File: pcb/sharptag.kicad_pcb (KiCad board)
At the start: 2 copper layers, 76.9 x 56.2 mm, 93 parts, among them J1 USB_C_Receptacle_USB2.0, J2 Conn_01x10, J3 Conn_01x02, J4 Conn_01x04, J5 Conn_01x03, J6 Conn_01x03, Q1 DMG3415U-7, Q2 DMG3415U-7, Q3 DMG3415U-7, Q4 Q_Photo_NPN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

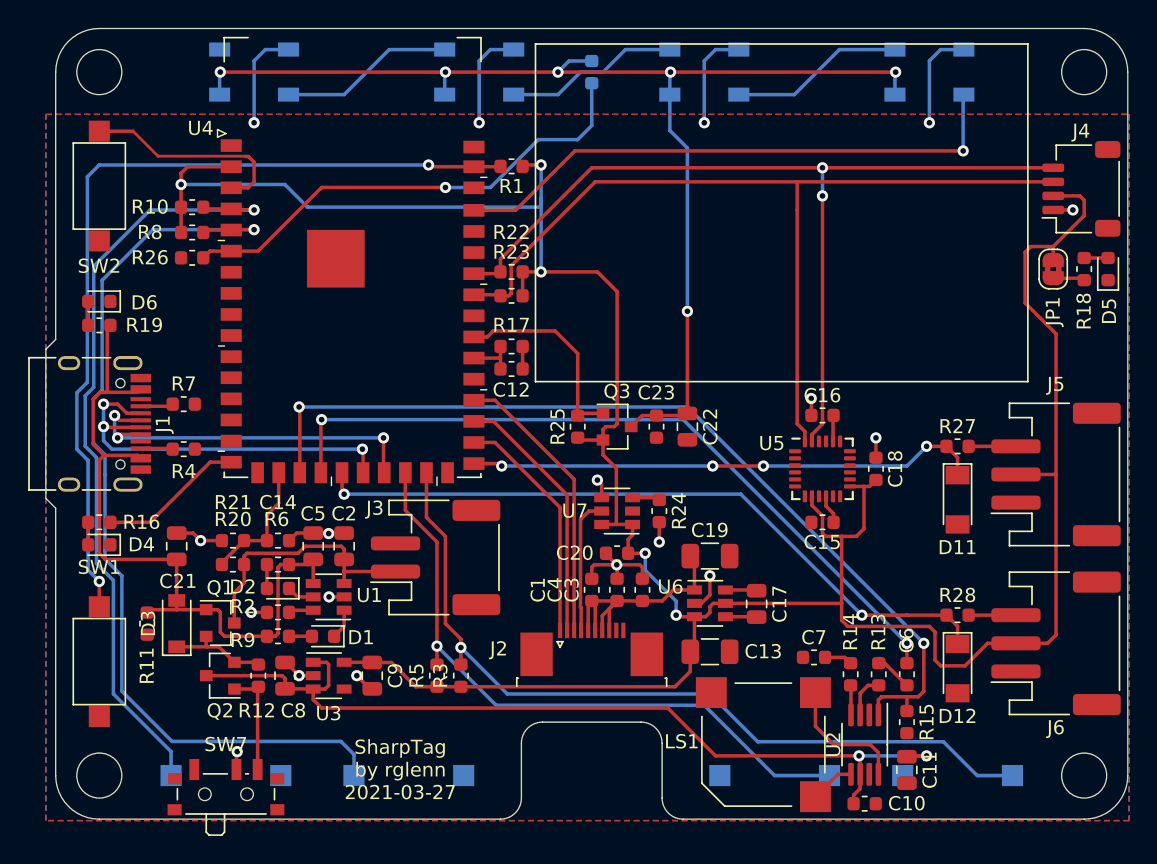
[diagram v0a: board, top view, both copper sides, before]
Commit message: Added tooling holes.
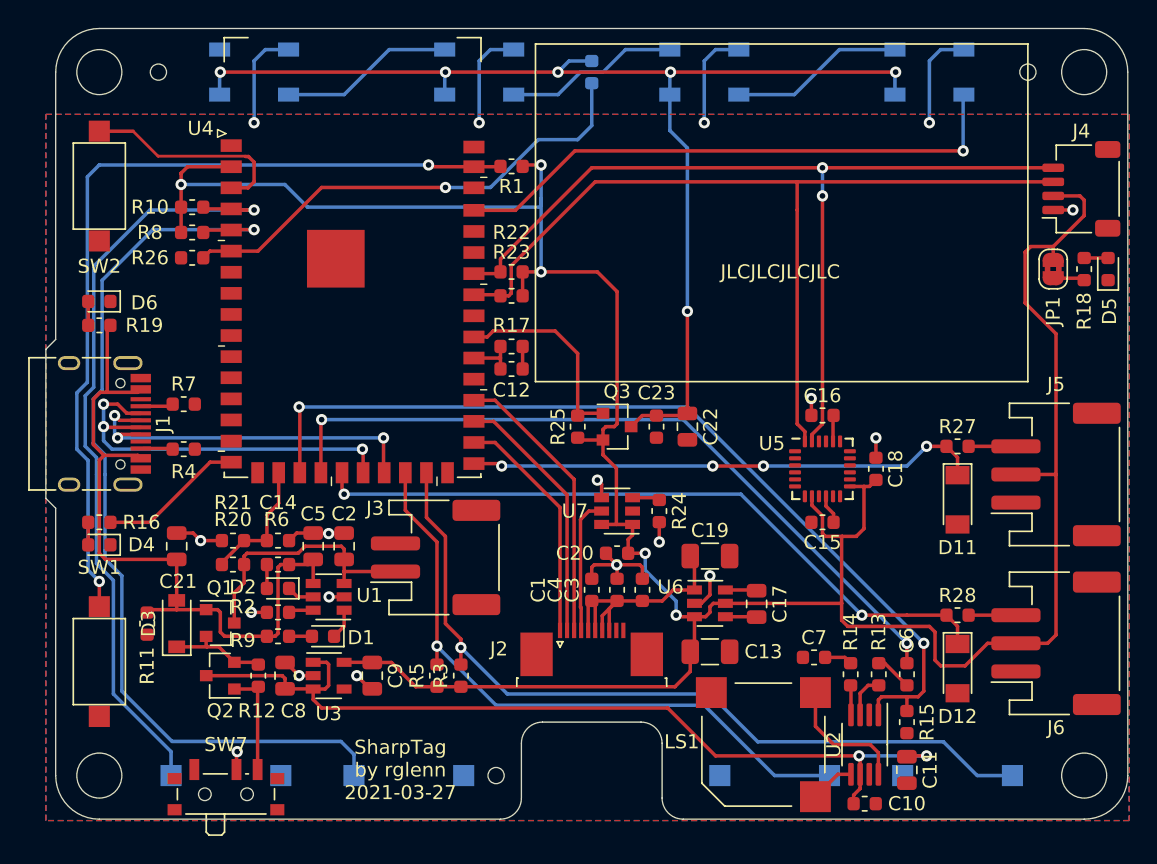
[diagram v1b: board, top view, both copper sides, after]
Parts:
- added H5: MountingHole, jlcpcb-tooling:tooling-hole, F.Cu at (-6.80, 27.0)
- added H6: MountingHole, jlcpcb-tooling:tooling-hole, F.Cu at (-30.8, -23.0)
- added H7: MountingHole, jlcpcb-tooling:tooling-hole, F.Cu at (31.0, -23.0)
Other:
- board text added: "JLCJLCJLCJLC"
